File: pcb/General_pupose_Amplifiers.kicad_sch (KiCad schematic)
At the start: 36 parts, among them J11 Conn_01x04_Pin, U1 AD8426ACPZ-R7, U2 AD8426ACPZ-R7

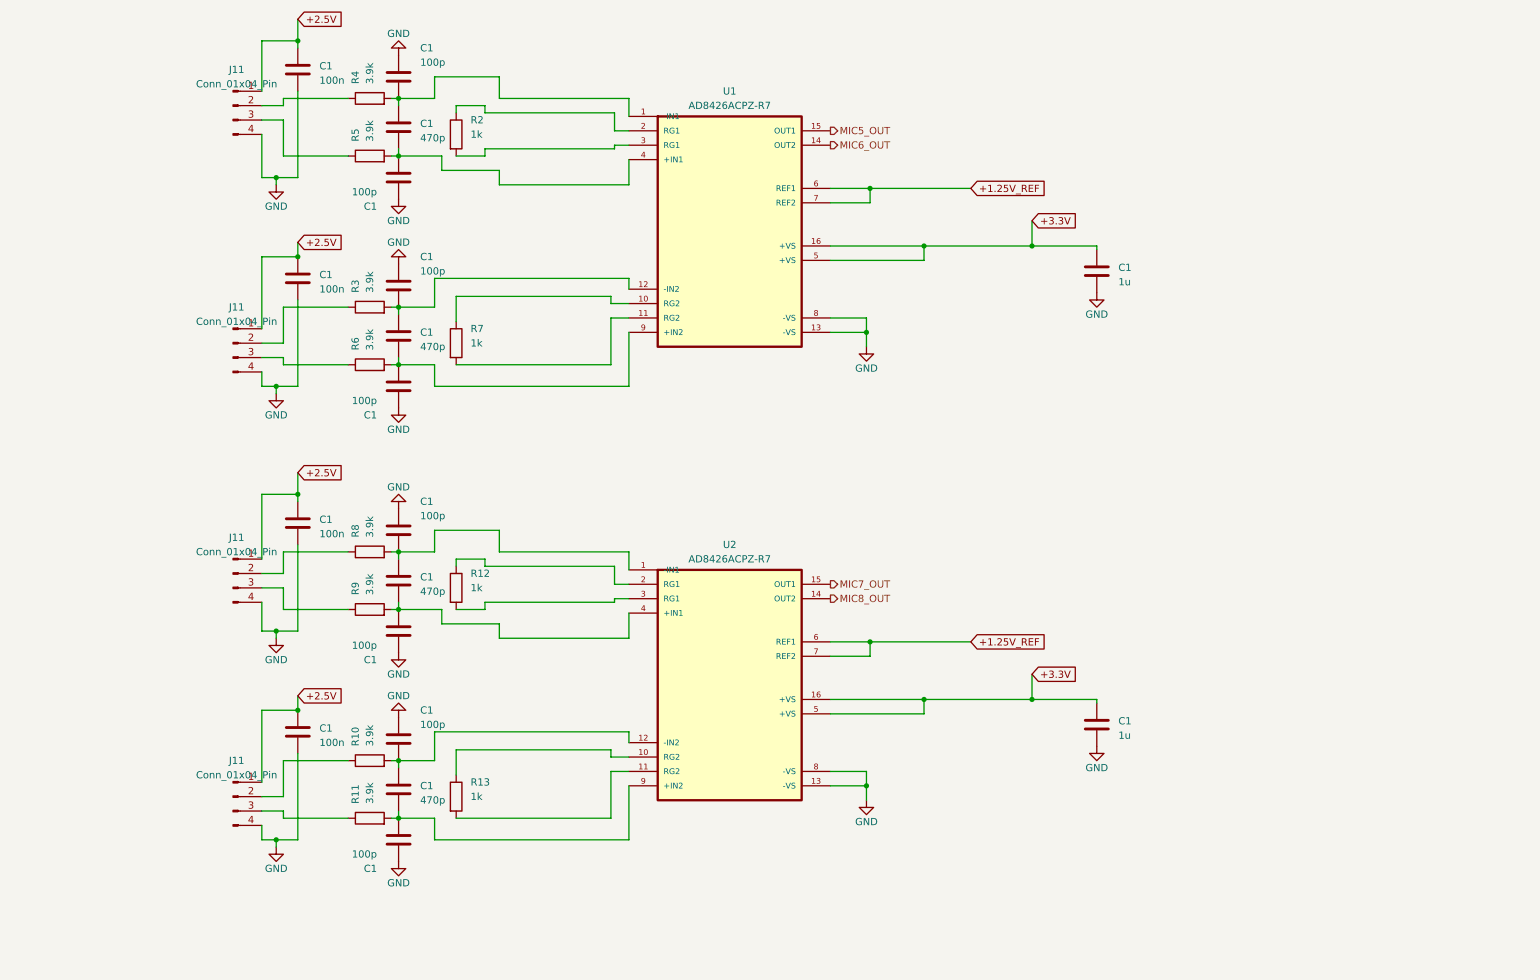
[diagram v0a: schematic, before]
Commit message: feat: Reorganize PCB project
Include all 3D step files
Refactor all folders for symbolds and footprints
Add missing datasheets
Link all symbols in KiCad projects
Rename the project to SensEdu
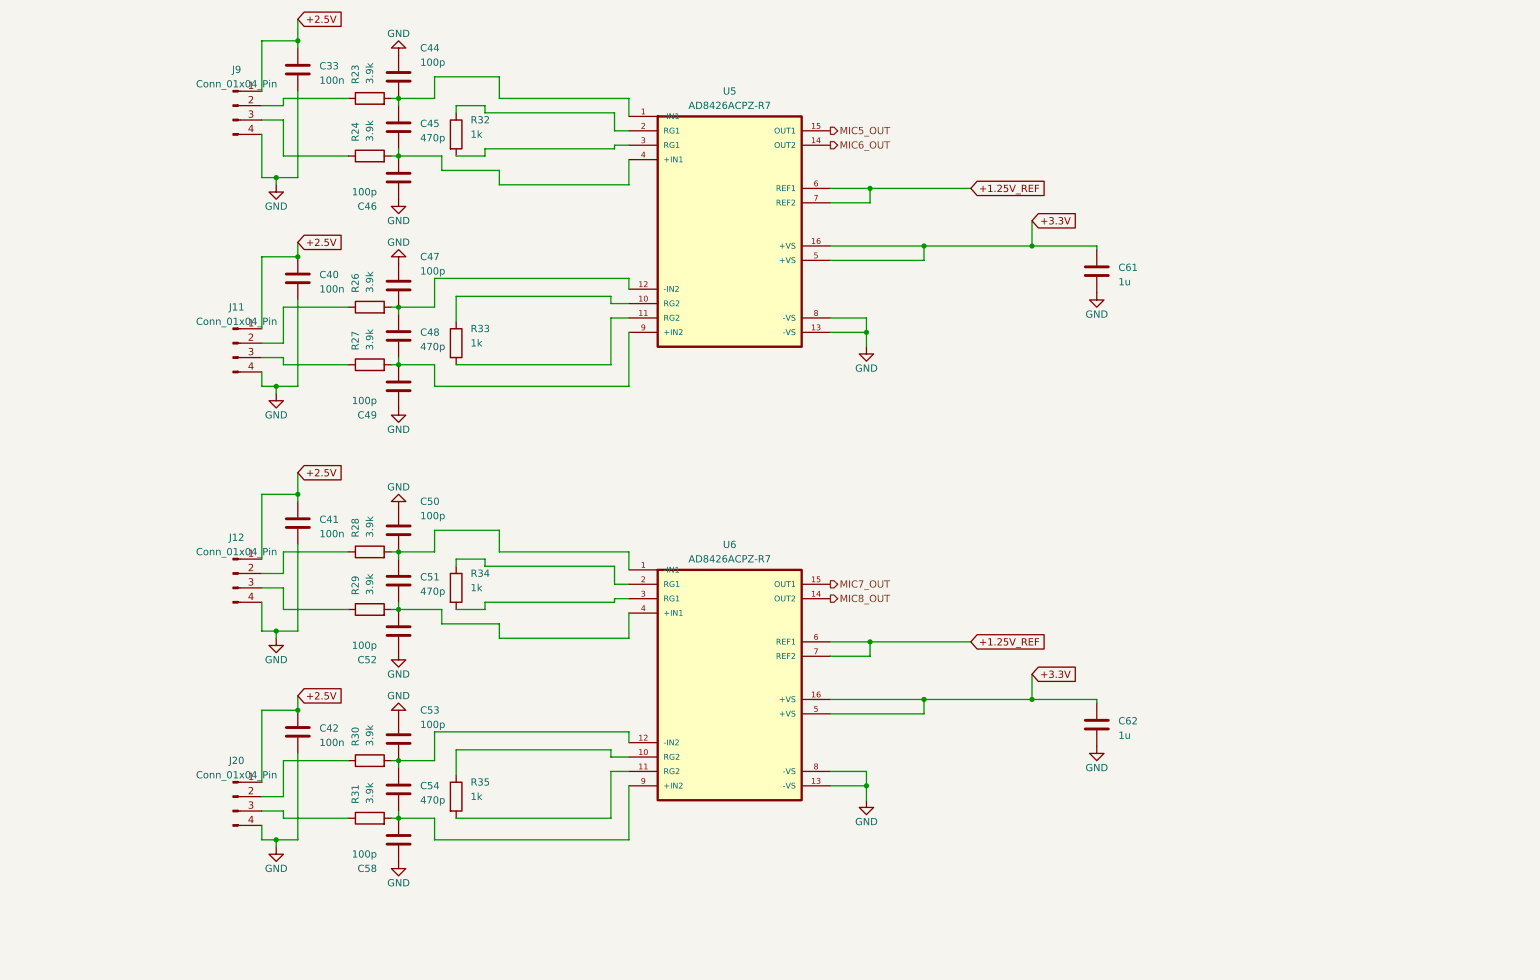
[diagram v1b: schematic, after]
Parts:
- renumbered C1 to C33, C1 to C40, C1 to C41, C1 to C42, C1 to C44, C1 to C45, C1 to C46, C1 to C47, C1 to C48, C1 to C49, C1 to C50, C1 to C51, C1 to C52, C1 to C53, C1 to C54, C1 to C58, C1 to C61, C1 to C62, J11 to J12, J11 to J20, J11 to J9, R4 to R23, R5 to R24, R3 to R26, R6 to R27, R8 to R28, R9 to R29, R10 to R30, R11 to R31, R2 to R32, R7 to R33, R12 to R34, R13 to R35, U1 to U5, U2 to U6

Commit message: feat: fix DRC and ERC errors and warnings
first clean version
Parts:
- removed U5, U6: AD8426ACPZ-R7, AD8426:QFN65P400X400X100-16N, symbol AD8222ACPZ-RL:AD8222ACPZ-RL
- added U5, U6: AD8426ACPZ-R7, SensEdu:QFN65P400X400X100-16N, symbol SensEdu:AD8426ACPZ-R7
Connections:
- net +1.25V_REF: now also U5.6 (REF1), U5.7 (REF2), U6.6 (REF1), U6.7 (REF2)
- net +3.3V: now also U5.16 (+VS), U5.5 (+VS_2), U6.16 (+VS), U6.5 (+VS_2)
- net GND: now also U5.13 (-VS_2), U5.8 (-VS), U6.13 (-VS_2), U6.8 (-VS)
- net MIC5_OUT: now also U5.15 (OUT1)
- net MIC6_OUT: now also U5.14 (OUT2)
- net MIC7_OUT: now also U6.15 (OUT1)
- net MIC8_OUT: now also U6.14 (OUT2)
- net at C48.2, C49.2, R27.2: now also U5.9 (+IN2)
- net at C47.2, C48.1, R26.2: now also U5.12 (-IN2)
- net at C50.2, C51.1, R28.2: now also U6.1 (-IN1)
- net at R35.1: now also U6.10 (RG2_2)
- net at R35.2: now also U6.11 (RG2)
- net at C53.2, C54.1, R30.2: now also U6.12 (-IN2)
- net at R34.1: now also U6.2 (RG1_2)
- net at R34.2: now also U6.3 (RG1)
- net at C51.2, C52.2, R29.2: now also U6.4 (+IN1)
- net at C54.2, C58.2, R31.2: now also U6.9 (+IN2)
- net at R32.1: now also U5.2 (RG1_2)
- net at R32.2: now also U5.3 (RG1)
- net at C44.2, C45.1, R23.2: now also U5.1 (-IN1)
- net at C45.2, C46.2, R24.2: now also U5.4 (+IN1)
- net at R33.1: now also U5.10 (RG2_2)
- net at R33.2: now also U5.11 (RG2)
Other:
- moved on the sheet: C33, C40, C41, C42, C44, C45, C46, C47, C48, C49, C50, C51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

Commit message: Polishin pt1
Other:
- company: (none) -> Infineon Technologies
- title: (none) -> SensEdu 0.7
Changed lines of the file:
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@@
 	(generator_version "9.0")
 	(paper "A4")
+	(title_block
+		(title "SensEdu 0.7")
+		(date "2025-12-05")
+		(company "Infineon Technologies")
+		(comment 1 "Author: Arshad Pattathil/Harald Gietler/Azra Talic")
+	)
 	(junction
 		(at 127 24.13)

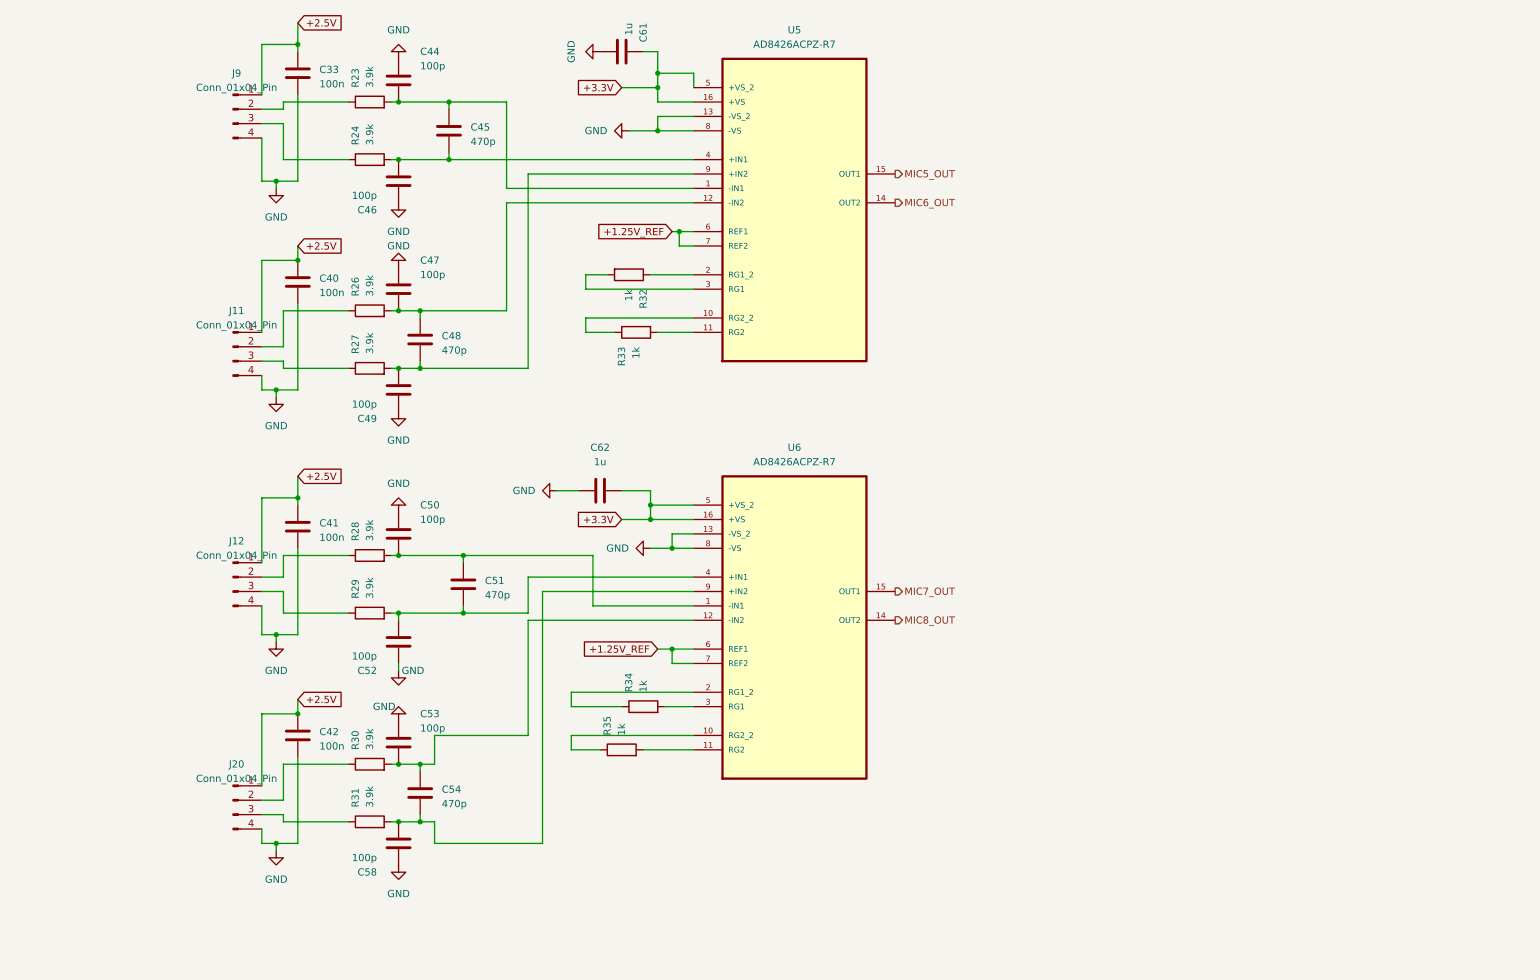
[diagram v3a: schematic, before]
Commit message: feat: Polished Sensedu schematics
Renamed Sheets
Added Nets
Repaired connections
Renamed Datasheets
Generated new schematic PDF
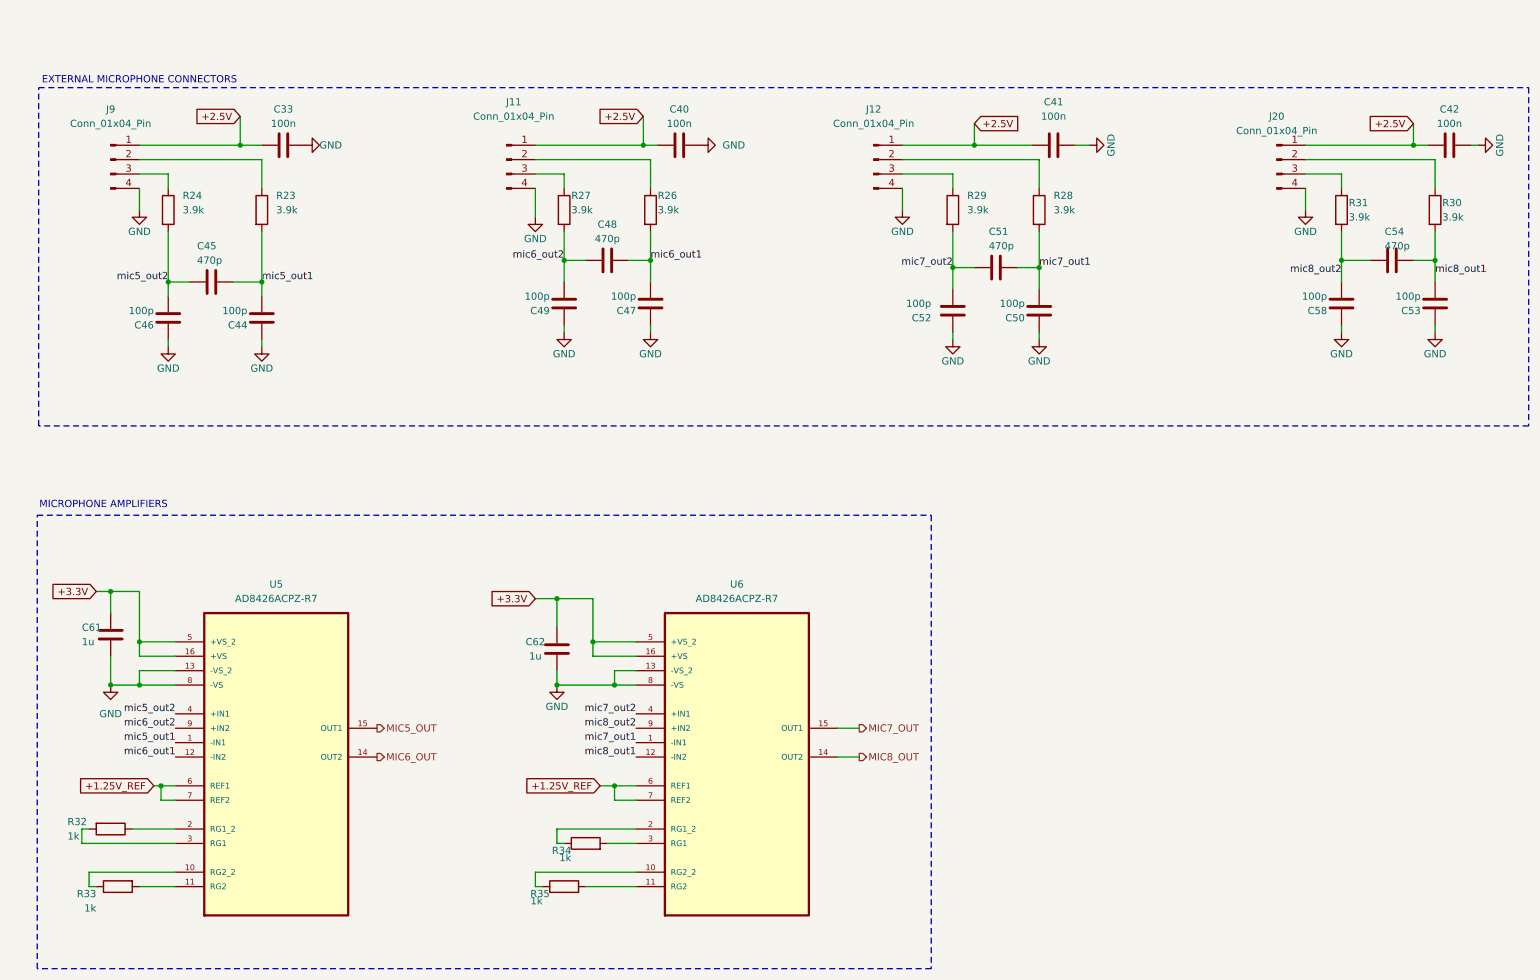
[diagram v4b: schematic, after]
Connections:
- net mic7_out1: now reaches C50.2, C51.1, R28.2, U6.1 (-IN1)
- net mic8_out1: now reaches C53.2, C54.1, R30.2, U6.12 (-IN2)
- net mic7_out2: now reaches C51.2, C52.2, R29.2, U6.4 (+IN1)
- net mic8_out2: now reaches C54.2, C58.2, R31.2, U6.9 (+IN2)
- net mic6_out2: now reaches C48.2, C49.2, R27.2, U5.9 (+IN2)
- net mic6_out1: now reaches C47.2, C48.1, R26.2, U5.12 (-IN2)
- net mic5_out1: now reaches C44.2, C45.1, R23.2, U5.1 (-IN1)
- net mic5_out2: now reaches C45.2, C46.2, R24.2, U5.4 (+IN1)
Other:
- note added: "EXTERNAL MICROPHONE CONNECTORS"
- note added: "MICROPHONE AMPLIFIERS"
- moved on the sheet: C33, C40, C41, C42, C44, C45, C46, C47, C48, C49, C50, C51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

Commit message: refactor: Edit speaker/mic symbols and polish
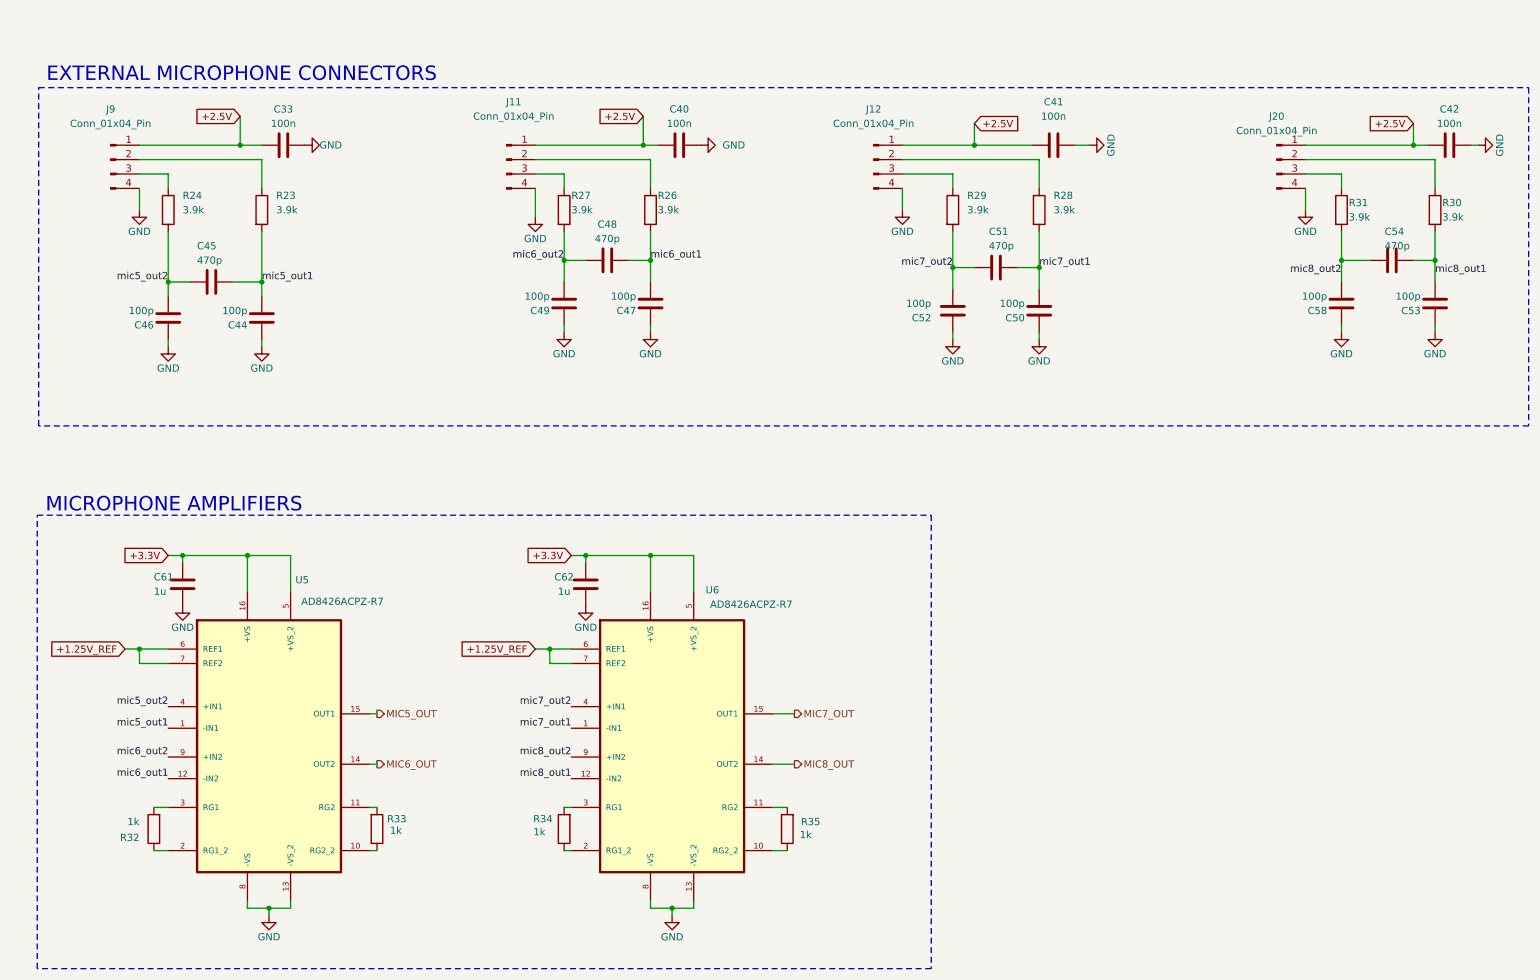
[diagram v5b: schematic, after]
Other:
- moved on the sheet: C61, C62, R32, R33, R34, R35, U5, U6
